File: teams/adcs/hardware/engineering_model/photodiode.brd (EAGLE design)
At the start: 25.4 x 34.3 mm, 13 parts, among them U1 LTC2483IDD

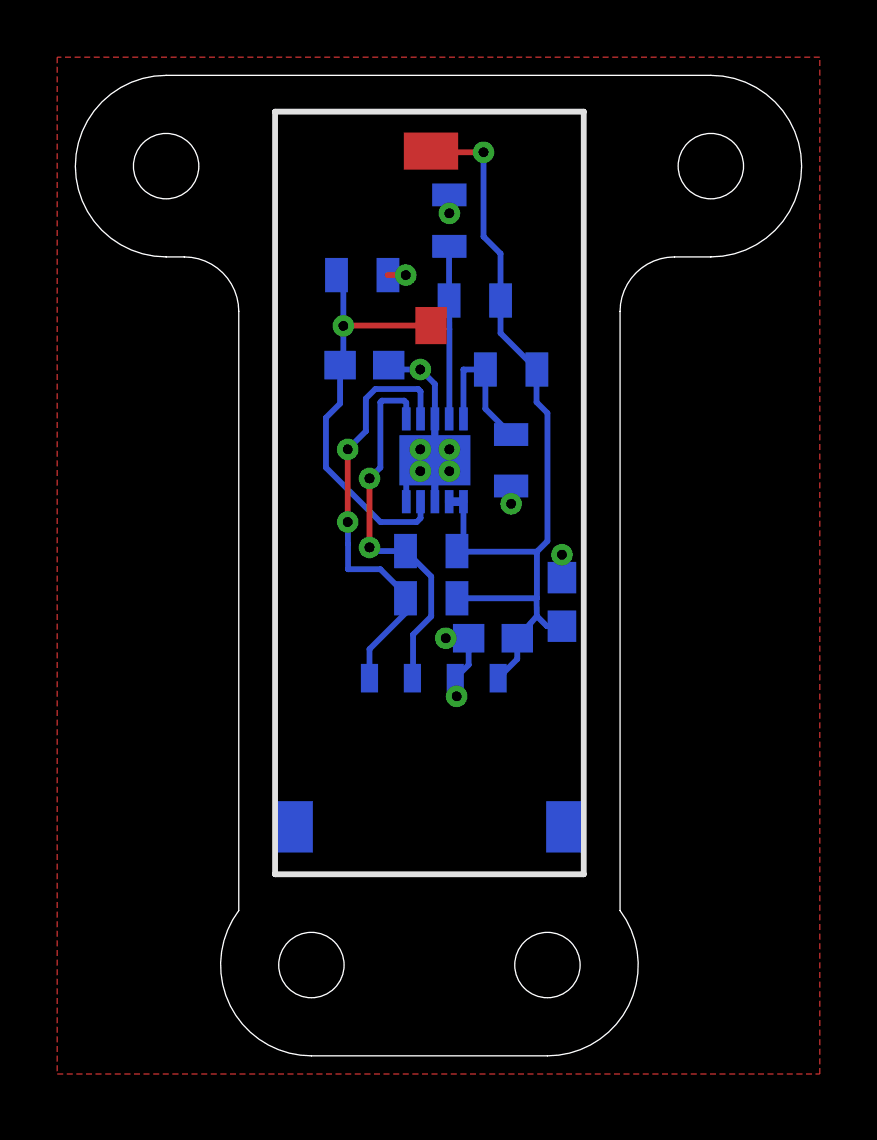
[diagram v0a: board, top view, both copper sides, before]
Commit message: Added extra silkscreen to annotate mounting
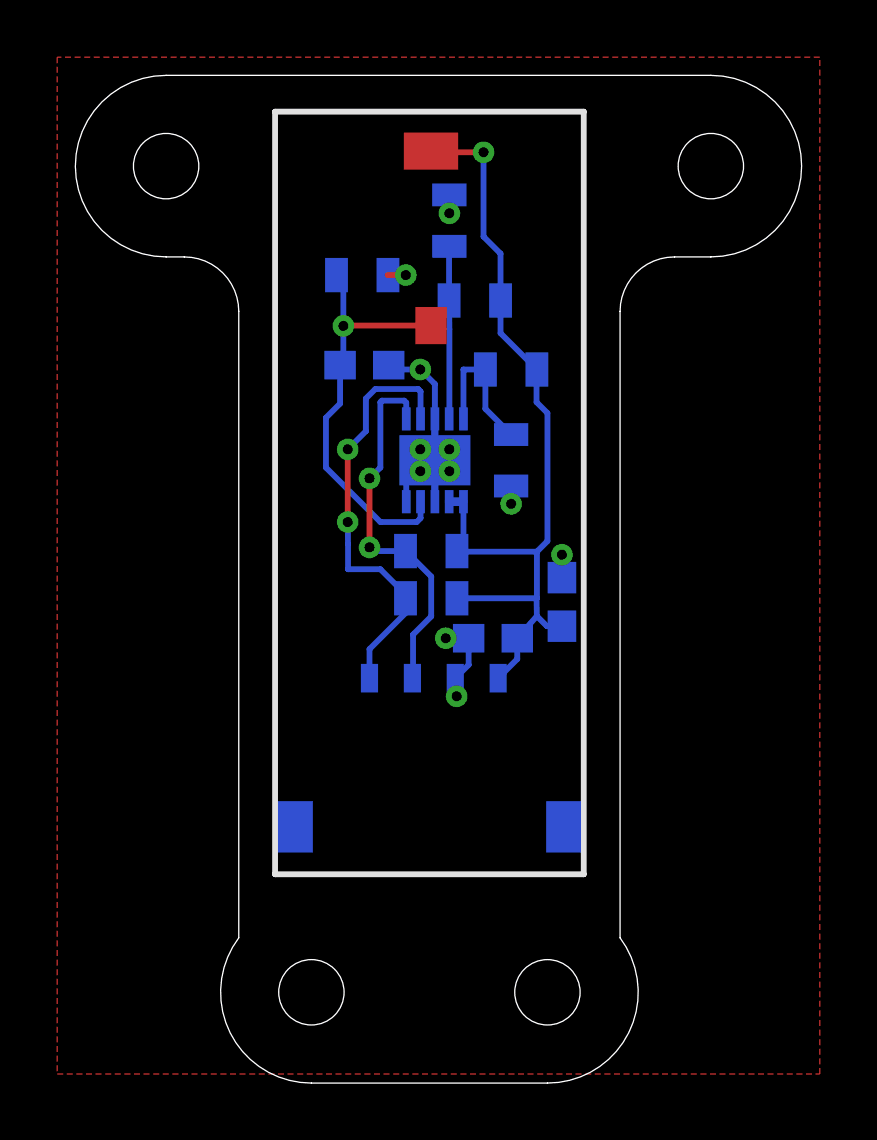
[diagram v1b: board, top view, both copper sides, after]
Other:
- board size 25.4 x 34.3 mm -> 25.4 x 35.2 mm
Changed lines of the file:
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@@
 <setting verticaltext="up"/>
 </settings>
-<grid distance="25" unitdist="mil" unit="mil" style="lines" multiple="1" display="yes" altdistance="5" altunitdist="mil" altunit="mil"/>
+<grid distance="12.5" unitdist="mil" unit="mil" style="lines" multiple="1" display="yes" altdistance="5" altunitdist="mil" altunit="mil"/>
 <layers>
 <layer number="1" name="Top" color="4" fill="1" visible="yes" active="yes"/>
@@
 <plain>
 <wire x1="17.145" y1="34.29" x2="-1.905" y2="34.29" width="0" layer="20"/>
-<hole x="3.175" y="3.175" drill="2.286"/>
-<hole x="11.43" y="3.175" drill="2.286"/>
+<hole x="3.175" y="2.2225" drill="2.286"/>
+<hole x="11.43" y="2.2225" drill="2.286"/>
 <hole x="17.145" y="31.115" drill="2.286"/>
 <hole x="-1.905" y="31.115" drill="2.286"/>
 <wire x1="-1.905" y1="27.94" x2="-1.27" y2="27.94" width="0" layer="20"/>
 <wire x1="-1.27" y1="27.94" x2="0.635" y2="26.035" width="0" layer="20" curve="-90"/>
-<wire x1="0.635" y1="26.035" x2="0.635" y2="5.08" width="0" layer="20"/>
+<wire x1="0.635" y1="26.035" x2="0.635" y2="4.1275" width="0" layer="20"/>
 <wire x1="17.145" y1="27.94" x2="15.875" y2="27.94" width="0" layer="20"/>
 <wire x1="15.875" y1="27.94" x2="13.97" y2="26.035" width="0" layer="20" curve="90"/>
-<wire x1="13.97" y1="26.035" x2="13.97" y2="5.08" width="0" layer="20"/>
+<wire x1="13.97" y1="26.035" x2="13.97" y2="4.1275" width="0" layer="20"/>
 <wire x1="-1.905" y1="34.29" x2="-1.905" y2="27.94" width="0" layer="20" curve="180"/>
 <wire x1="17.145" y1="34.29" x2="17.145" y2="27.94" width="0" layer="20" curve="-180"/>
-<wire x1="3.175" y1="0" x2="11.43" y2="0" width="0" layer="20"/>
-<wire x1="3.175" y1="0" x2="0.635" y2="5.08" width="0" layer="20" curve="-126.869898"/>
-<wire x1="11.43" y1="0" x2="13.97" y2="5.08" width="0" layer="20" curve="126.869898"/>
+<wire x1="3.175" y1="-0.9525" x2="11.43" y2="-0.9525" width="0" layer="20"/>
+<wire x1="3.175" y1="-0.9525" x2="0.635" y2="4.1275" width="0" layer="20" curve="-126.869898"/>
+<wire x1="11.43" y1="-0.9525" x2="13.97" y2="4.1275" width="0" layer="20" curve="126.869898"/>
 <wire x1="1.905" y1="6.35" x2="12.7" y2="6.35" width="0.2032" layer="112"/>
 <wire x1="1.905" y1="6.35" x2="1.905" y2="33.02" width="0.2032" layer="112"/>
 <wire x1="12.7" y1="6.35" x2="12.7" y2="33.02" width="0.2032" layer="112"/>
 <wire x1="1.905" y1="33.02" x2="12.7" y2="33.02" width="0.2032" layer="112"/>
+<circle x="-1.905" y="31.115" radius="2.3876" width="0.1524" layer="49"/>
+<circle x="17.145" y="31.115" radius="2.3876" width="0.1524" layer="49"/>
+<circle x="3.175" y="2.2225" radius="2.3876" width="0.1524" layer="49"/>
+<circle x="11.43" y="2.2225" radius="2.3876" width="0.1524" layer="49"/>
 </plain>
 <attributes>

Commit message: Add extra silkscreen to annotate mounting
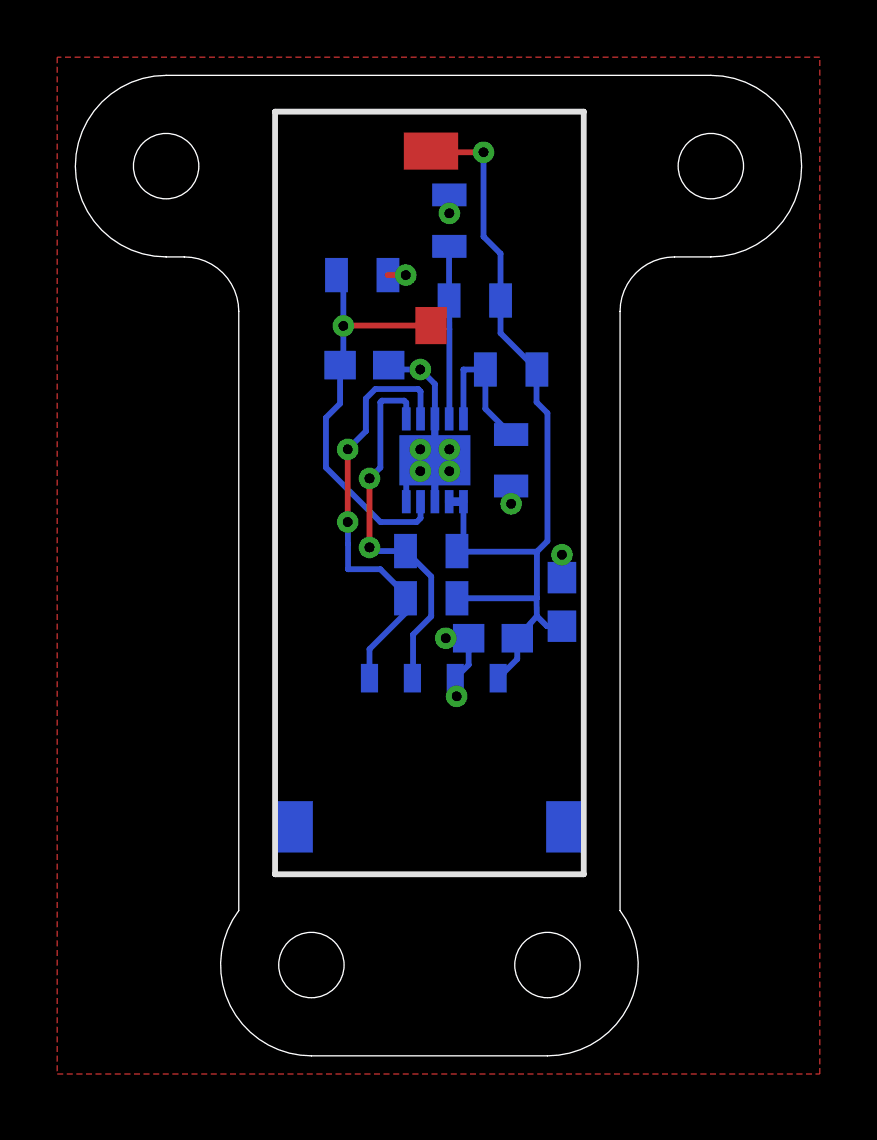
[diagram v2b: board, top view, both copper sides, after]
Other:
- board size 25.4 x 35.2 mm -> 25.4 x 34.3 mm
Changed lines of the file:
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@@
 <setting verticaltext="up"/>
 </settings>
-<grid distance="12.5" unitdist="mil" unit="mil" style="lines" multiple="1" display="yes" altdistance="5" altunitdist="mil" altunit="mil"/>
+<grid distance="25" unitdist="mil" unit="mil" style="lines" multiple="1" display="yes" altdistance="5" altunitdist="mil" altunit="mil"/>
 <layers>
 <layer number="1" name="Top" color="4" fill="1" visible="yes" active="yes"/>
@@
 <plain>
 <wire x1="17.145" y1="34.29" x2="-1.905" y2="34.29" width="0" layer="20"/>
-<hole x="3.175" y="2.2225" drill="2.286"/>
-<hole x="11.43" y="2.2225" drill="2.286"/>
+<hole x="3.175" y="3.175" drill="2.286"/>
+<hole x="11.43" y="3.175" drill="2.286"/>
 <hole x="17.145" y="31.115" drill="2.286"/>
 <hole x="-1.905" y="31.115" drill="2.286"/>
 <wire x1="-1.905" y1="27.94" x2="-1.27" y2="27.94" width="0" layer="20"/>
 <wire x1="-1.27" y1="27.94" x2="0.635" y2="26.035" width="0" layer="20" curve="-90"/>
-<wire x1="0.635" y1="26.035" x2="0.635" y2="4.1275" width="0" layer="20"/>
+<wire x1="0.635" y1="26.035" x2="0.635" y2="5.08" width="0" layer="20"/>
 <wire x1="17.145" y1="27.94" x2="15.875" y2="27.94" width="0" layer="20"/>
 <wire x1="15.875" y1="27.94" x2="13.97" y2="26.035" width="0" layer="20" curve="90"/>
-<wire x1="13.97" y1="26.035" x2="13.97" y2="4.1275" width="0" layer="20"/>
+<wire x1="13.97" y1="26.035" x2="13.97" y2="5.08" width="0" layer="20"/>
 <wire x1="-1.905" y1="34.29" x2="-1.905" y2="27.94" width="0" layer="20" curve="180"/>
 <wire x1="17.145" y1="34.29" x2="17.145" y2="27.94" width="0" layer="20" curve="-180"/>
-<wire x1="3.175" y1="-0.9525" x2="11.43" y2="-0.9525" width="0" layer="20"/>
-<wire x1="3.175" y1="-0.9525" x2="0.635" y2="4.1275" width="0" layer="20" curve="-126.869898"/>
-<wire x1="11.43" y1="-0.9525" x2="13.97" y2="4.1275" width="0" layer="20" curve="126.869898"/>
+<wire x1="3.175" y1="0" x2="11.43" y2="0" width="0" layer="20"/>
+<wire x1="3.175" y1="0" x2="0.635" y2="5.08" width="0" layer="20" curve="-126.869898"/>
+<wire x1="11.43" y1="0" x2="13.97" y2="5.08" width="0" layer="20" curve="126.869898"/>
 <wire x1="1.905" y1="6.35" x2="12.7" y2="6.35" width="0.2032" layer="112"/>
 <wire x1="1.905" y1="6.35" x2="1.905" y2="33.02" width="0.2032" layer="112"/>
 <wire x1="12.7" y1="6.35" x2="12.7" y2="33.02" width="0.2032" layer="112"/>
 <wire x1="1.905" y1="33.02" x2="12.7" y2="33.02" width="0.2032" layer="112"/>
-<circle x="-1.905" y="31.115" radius="2.3876" width="0.1524" layer="49"/>
-<circle x="17.145" y="31.115" radius="2.3876" width="0.1524" layer="49"/>
-<circle x="3.175" y="2.2225" radius="2.3876" width="0.1524" layer="49"/>
-<circle x="11.43" y="2.2225" radius="2.3876" width="0.1524" layer="49"/>
 </plain>
 <attributes>
